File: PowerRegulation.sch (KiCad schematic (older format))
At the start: 6 parts

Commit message: Annotation completed
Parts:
- gave numbers to parts that had none: 6
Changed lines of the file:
@@
 $EndDescr
 $Comp
-L GND #PWR?
+L GND #PWR401
 U 1 1 57DB72C4
 P 6500 4500
-F 0 "#PWR?" H 6500 4250 50  0001 C CNN
+F 0 "#PWR401" H 6500 4250 50  0001 C CNN
 F 1 "GND" H 6500 4350 50  0000 C CNN
 F 2 "" H 6500 4500 50  0000 C CNN
@@
 $EndComp
 $Comp
-L C C?
+L C C401
 U 1 1 57DB72CA
 P 5650 4150
-F 0 "C?" H 5675 4250 50  0000 L CNN
+F 0 "C401" H 5675 4250 50  0000 L CNN
 F 1 "C" H 5675 4050 50  0000 L CNN
 F 2 "" H 5688 4000 50  0000 C CNN
@@
 $EndComp
 $Comp
-L C C?
+L C C402
 U 1 1 57DB72D1
 P 7650 4350
-F 0 "C?" H 7675 4450 50  0000 L CNN
+F 0 "C402" H 7675 4450 50  0000 L CNN
 F 1 "C" H 7675 4250 50  0000 L CNN
 F 2 "" H 7688 4200 50  0000 C CNN
@@
 $EndComp
 $Comp
-L R R?
+L R R401
 U 1 1 57DB72D8
 P 5950 4200
-F 0 "R?" V 6030 4200 50  0000 C CNN
+F 0 "R401" V 6030 4200 50  0000 C CNN
 F 1 "0" V 5950 4200 50  0000 C CNN
 F 2 "" V 5880 4200 50  0000 C CNN
@@
 $EndComp
 $Comp
-L LM2931D-R U?
+L LM2931D-R U401
 U 1 1 57DB72DF
 P 6500 4200
-F 0 "U?" H 6800 4300 50  0000 C CNN
+F 0 "U401" H 6800 4300 50  0000 C CNN
 F 1 "LM2931D-R" H 6500 4800 50  0000 C CNN
 F 2 "" H 6500 4200 50  0000 C CNN
@@
 $EndComp
 $Comp
-L R R?
+L R R402
 U 1 1 57DB72E6
 P 7300 3900
-F 0 "R?" V 7380 3900 50  0000 C CNN
+F 0 "R402" V 7380 3900 50  0000 C CNN
 F 1 "27k" V 7300 3900 50  0000 C CNN
 F 2 "" V 7230 3900 50  0000 C CNN
@@
 $EndComp
 $Comp
-L R R?
+L R R403
 U 1 1 57DB72ED
 P 7300 4350
-F 0 "R?" V 7380 4350 50  0000 C CNN
+F 0 "R403" V 7380 4350 50  0000 C CNN
 F 1 "21.6k" V 7300 4350 50  0000 C CNN
 F 2 "" V 7230 4350 50  0000 C CNN

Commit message: Add initial layout
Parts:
- C401, C402: footprint (none) -> Capacitors_SMD:C_0805
- R401, R402, R403: footprint (none) -> Resistors_SMD:R_0805
- U401: footprint (none) -> SMD_Packages:SOIC-8-N
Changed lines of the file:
@@
 $EndDescr
 $Comp
-L GND #PWR401
+L GND #PWR07
 U 1 1 57DB72C4
 P 6500 4500
-F 0 "#PWR401" H 6500 4250 50  0001 C CNN
+F 0 "#PWR07" H 6500 4250 50  0001 C CNN
 F 1 "GND" H 6500 4350 50  0000 C CNN
 F 2 "" H 6500 4500 50  0000 C CNN
@@
 F 0 "C401" H 5675 4250 50  0000 L CNN
 F 1 "C" H 5675 4050 50  0000 L CNN
-F 2 "" H 5688 4000 50  0000 C CNN
+F 2 "Capacitors_SMD:C_0805" H 5688 4000 50  0001 C CNN
 F 3 "" H 5650 4150 50  0000 C CNN
 	1    5650 4150
@@
 F 0 "C402" H 7675 4450 50  0000 L CNN
 F 1 "C" H 7675 4250 50  0000 L CNN
-F 2 "" H 7688 4200 50  0000 C CNN
+F 2 "Capacitors_SMD:C_0805" H 7688 4200 50  0001 C CNN
 F 3 "" H 7650 4350 50  0000 C CNN
 	1    7650 4350
@@
 F 0 "R401" V 6030 4200 50  0000 C CNN
 F 1 "0" V 5950 4200 50  0000 C CNN
-F 2 "" V 5880 4200 50  0000 C CNN
+F 2 "Resistors_SMD:R_0805" V 5880 4200 50  0001 C CNN
 F 3 "" H 5950 4200 50  0000 C CNN
 	1    5950 4200
@@
 F 0 "U401" H 6800 4300 50  0000 C CNN
 F 1 "LM2931D-R" H 6500 4800 50  0000 C CNN
-F 2 "" H 6500 4200 50  0000 C CNN
+F 2 "SMD_Packages:SOIC-8-N" H 6500 4200 50  0001 C CNN
 F 3 "http://www.st.com/content/ccc/resource/technical/document/datasheet/ae/39/36/68/10/73/4f/bb/CD00001885.pdf/files/CD00001885.pdf/jcr:content/translations/en.CD00001885.pdf" H 6500 4200 50  0001 C CNN
 	1    6500 4200
@@
 F 0 "R402" V 7380 3900 50  0000 C CNN
 F 1 "27k" V 7300 3900 50  0000 C CNN
-F 2 "" V 7230 3900 50  0000 C CNN
+F 2 "Resistors_SMD:R_0805" V 7230 3900 50  0001 C CNN
 F 3 "" H 7300 3900 50  0000 C CNN
 	1    7300 3900
@@
 F 0 "R403" V 7380 4350 50  0000 C CNN
 F 1 "21.6k" V 7300 4350 50  0000 C CNN
-F 2 "" V 7230 4350 50  0000 C CNN
+F 2 "Resistors_SMD:R_0805" V 7230 4350 50  0001 C CNN
 F 3 "" H 7300 4350 50  0000 C CNN
 	1    7300 4350

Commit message: Add heat sink footprint
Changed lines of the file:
@@
 	-1   0    0    -1
 $EndComp
+Text GLabel 8200 3750 2    60   Input ~ 0
+2.7V
+Text HLabel 5450 3750 0    60   Input ~ 0
+Vin
 Wire Wire Line
 	8200 3750 6950 3750
@@
 Connection ~ 7300 4500
 Wire Wire Line
-	6650 4350 6350 4350
-Connection ~ 6550 4350
-Connection ~ 6450 4350
-Wire Wire Line
 	6500 4500 6500 4350
-Connection ~ 6500 4350
 Wire Wire Line
 	5650 4500 5650 4300
@@
 	6050 3750 5450 3750
 Connection ~ 5650 3750
-Text GLabel 8200 3750 2    60   Input ~ 0
-2.7V
-Text HLabel 5450 3750 0    60   Input ~ 0
-Vin
+Wire Wire Line
+	6350 4350 6650 4350
+Connection ~ 6550 4350
+Connection ~ 6500 4350
+Connection ~ 6450 4350
 $EndSCHEMATC

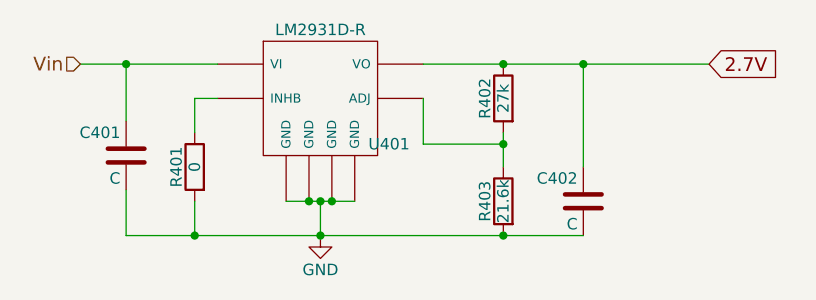
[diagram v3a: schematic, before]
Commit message: Add potentiometers
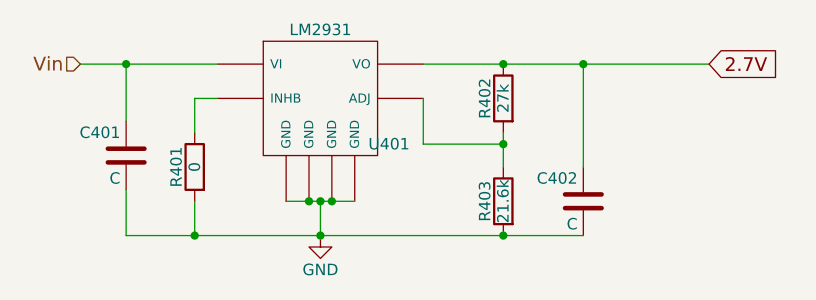
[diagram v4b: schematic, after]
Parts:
- U401: value LM2931D-R -> LM2931; MPN (none) -> LM2931D-R
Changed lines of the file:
@@
 P 6500 4200
 F 0 "U401" H 6800 4300 50  0000 C CNN
-F 1 "LM2931D-R" H 6500 4800 50  0000 C CNN
+F 1 "LM2931" H 6500 4800 50  0000 C CNN
 F 2 "SMD_Packages:SOIC-8-N" H 6500 4200 50  0001 C CNN
 F 3 "http://www.st.com/content/ccc/resource/technical/document/datasheet/ae/39/36/68/10/73/4f/bb/CD00001885.pdf/files/CD00001885.pdf/jcr:content/translations/en.CD00001885.pdf" H 6500 4200 50  0001 C CNN
+F 4 "LM2931D-R" H 6500 4200 60  0001 C CNN "MPN"
 	1    6500 4200
 	1    0    0    -1

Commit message: Add preliminary BOM
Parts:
- C401, C402: value C -> .1
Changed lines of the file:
@@
 P 5650 4150
 F 0 "C401" H 5675 4250 50  0000 L CNN
-F 1 "C" H 5675 4050 50  0000 L CNN
+F 1 ".1" H 5675 4050 50  0000 L CNN
 F 2 "Capacitors_SMD:C_0805" H 5688 4000 50  0001 C CNN
 F 3 "" H 5650 4150 50  0000 C CNN
@@
 P 7650 4350
 F 0 "C402" H 7675 4450 50  0000 L CNN
-F 1 "C" H 7675 4250 50  0000 L CNN
+F 1 ".1" H 7675 4250 50  0000 L CNN
 F 2 "Capacitors_SMD:C_0805" H 7688 4200 50  0001 C CNN
 F 3 "" H 7650 4350 50  0000 C CNN

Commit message: Final schematic and BOM and layout
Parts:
- C401, C402: MPN (none) -> 08055C104KAT2A
- R401: MPN (none) -> RC0805JR-070RL
- R402: MPN (none) -> RMCF0805JT27K0
- R403: value 21.6k -> 21.5k; MPN (none) -> RC0805FR-0721K5L
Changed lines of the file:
@@
 F 1 ".1" H 5675 4050 50  0000 L CNN
 F 2 "Capacitors_SMD:C_0805" H 5688 4000 50  0001 C CNN
-F 3 "" H 5650 4150 50  0000 C CNN
+F 3 "http://datasheets.avx.com/X7RDielectric.pdf" H 5650 4150 50  0001 C CNN
+F 4 "08055C104KAT2A" H 5650 4150 60  0001 C CNN "MPN"
 	1    5650 4150
 	-1   0    0    -1
@@
 F 1 ".1" H 7675 4250 50  0000 L CNN
 F 2 "Capacitors_SMD:C_0805" H 7688 4200 50  0001 C CNN
-F 3 "" H 7650 4350 50  0000 C CNN
+F 3 "http://datasheets.avx.com/X7RDielectric.pdf" H 7650 4350 50  0001 C CNN
+F 4 "08055C104KAT2A" H 7650 4350 60  0001 C CNN "MPN"
 	1    7650 4350
 	-1   0    0    -1
@@
 F 1 "0" V 5950 4200 50  0000 C CNN
 F 2 "Resistors_SMD:R_0805" V 5880 4200 50  0001 C CNN
-F 3 "" H 5950 4200 50  0000 C CNN
+F 3 "http://www.yageo.com/NewPortal/yageodocoutput?fileName=/pdf/R-Chip/PYu-RC_Group_51_RoHS_L_4.pdf" H 5950 4200 50  0001 C CNN
+F 4 "RC0805JR-070RL" V 5950 4200 60  0001 C CNN "MPN"
 	1    5950 4200
 	-1   0    0    -1
@@
 F 1 "27k" V 7300 3900 50  0000 C CNN
 F 2 "Resistors_SMD:R_0805" V 7230 3900 50  0001 C CNN
-F 3 "" H 7300 3900 50  0000 C CNN
+F 3 "https://www.seielect.com/Catalog/SEI-RMCF_RMCP.pdf" H 7300 3900 50  0001 C CNN
+F 4 "RMCF0805JT27K0" V 7300 3900 60  0001 C CNN "MPN"
 	1    7300 3900
 	-1   0    0    -1
@@
 P 7300 4350
 F 0 "R403" V 7380 4350 50  0000 C CNN
-F 1 "21.6k" V 7300 4350 50  0000 C CNN
+F 1 "21.5k" V 7300 4350 50  0000 C CNN
 F 2 "Resistors_SMD:R_0805" V 7230 4350 50  0001 C CNN
-F 3 "" H 7300 4350 50  0000 C CNN
+F 3 "http://www.yageo.com/NewPortal/yageodocoutput?fileName=/pdf/R-Chip/PYu-RC_Group_51_RoHS_L_4.pdf" H 7300 4350 50  0001 C CNN
+F 4 "RC0805FR-0721K5L" V 7300 4350 60  0001 C CNN "MPN"
 	1    7300 4350
 	-1   0    0    -1
